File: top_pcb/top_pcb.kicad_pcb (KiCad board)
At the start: 2 copper layers, 50 x 50 mm, 17 parts, among them J1 flat_cable_connector, J2 header, J3 free_holes, J4 Conn_01x04

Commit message: Remove accidentaly connected gnd line to battery pad
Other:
- board text added: "Rev2020.06"
- board text removed: "Rev2020.05"

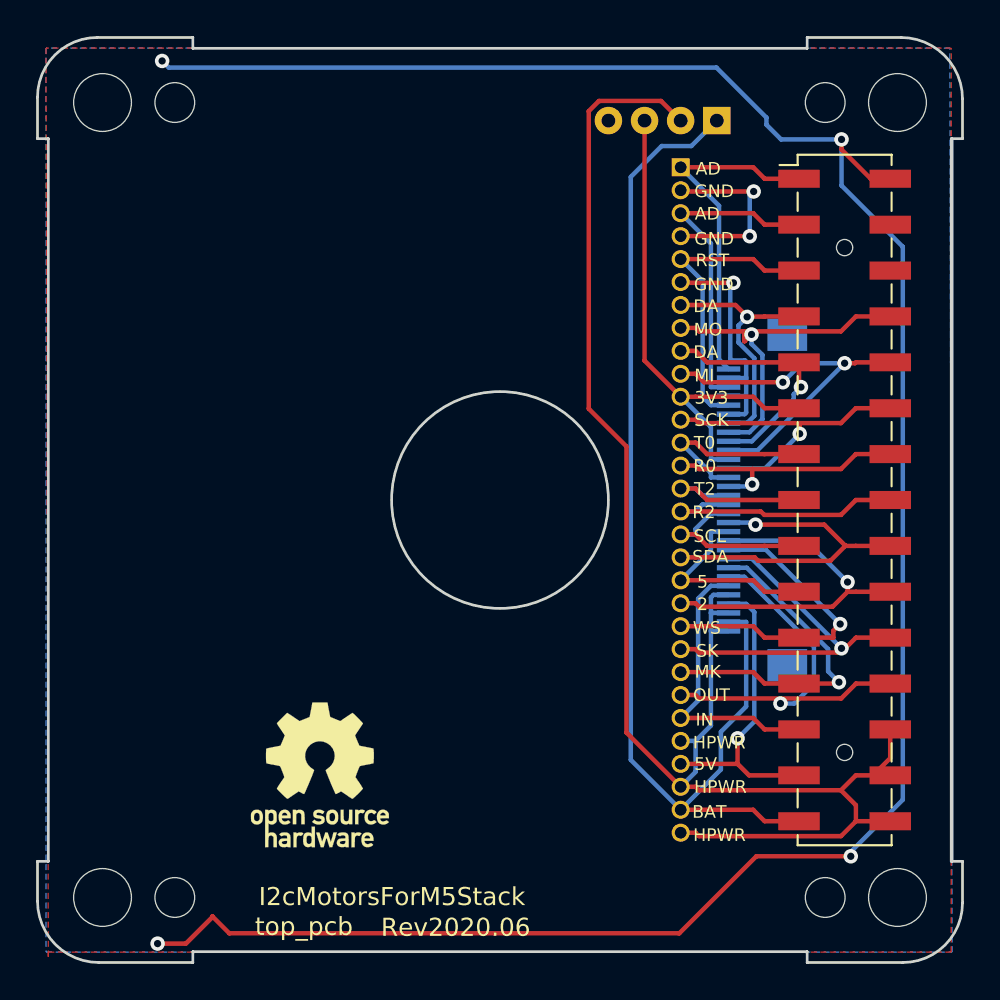
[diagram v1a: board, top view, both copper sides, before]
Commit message: Separate HPWR to NC0-2 for Core2
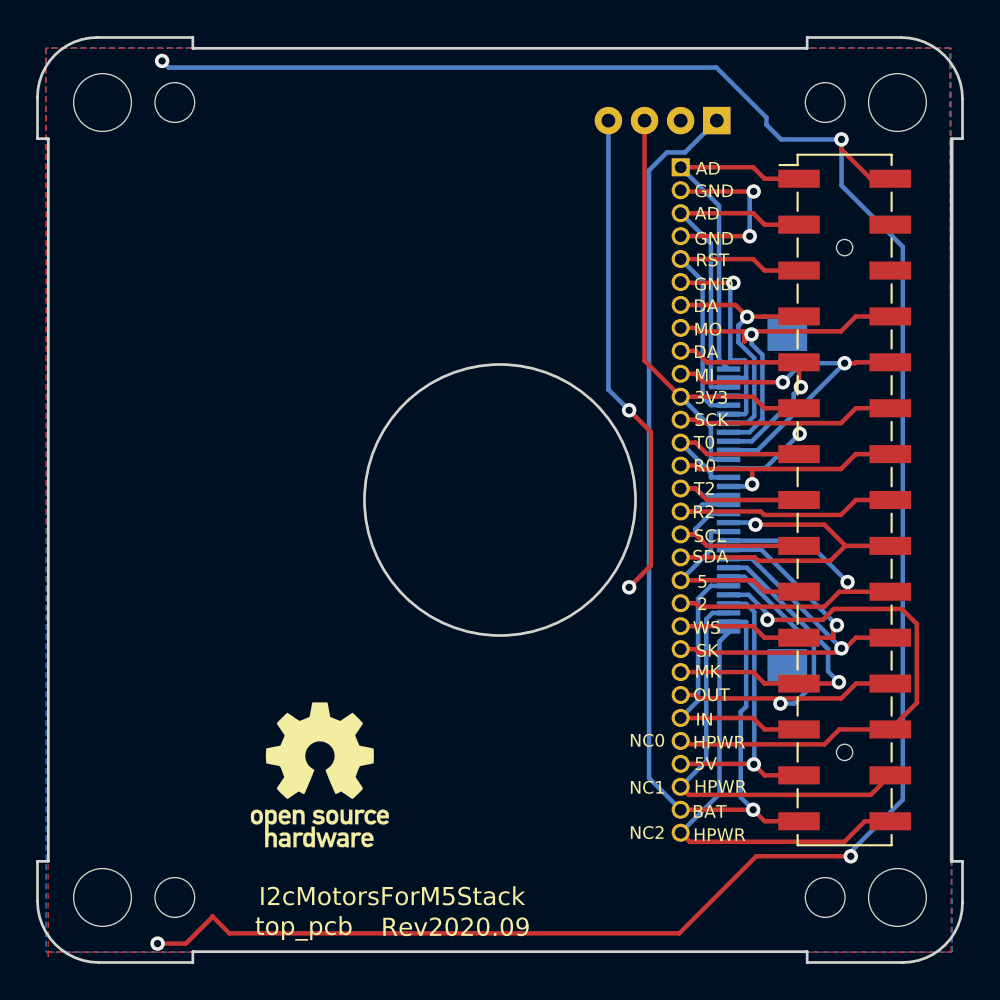
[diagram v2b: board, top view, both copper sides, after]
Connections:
- J1 pad 26: HPWR -> /NC0
- J1 pad 28: HPWR -> /NC1
- J1 pad 30: HPWR -> /NC2
- J2 pad 26: HPWR -> /NC0
- J2 pad 28: HPWR -> /NC1
- J2 pad 30: HPWR -> /NC2
- J3 pad 26: HPWR -> /NC0
- J3 pad 28: HPWR -> /NC1
- J3 pad 30: HPWR -> /NC2
- J4 pad 2: HPWR -> Net-(J4-Pad2)
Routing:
- net HPWR: track 89.5 -> 0.00 mm
- net /NC0: track 0.00 -> 30.3 mm, vias 0 -> 1
- net GND: track 151.4 -> 178.8 mm, vias 7 -> 9
- net /NC2: track 0.00 -> 24.8 mm
- net /NC1: track 0.00 -> 23.5 mm
- net +BATT: track 61.5 -> 59.6 mm, vias 0 -> 1
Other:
- outline, holes or cut-outs redrawn
- board text added: "NC0"
- board text added: "NC1"
- board text added: "NC2"
- board text added: "Rev2020.09"
- board text removed: "Rev2020.06"
